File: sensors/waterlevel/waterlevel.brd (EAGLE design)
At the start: 100 x 80 mm, 57 parts, among them IC1 LD117AS33TR, IC2 MCP604SL, IC3 MCP601SN, IC4 MCP601SN, P1 CAMDEN-CTB5000/6, U1 NCP1729SN35T1G, U2 SR05S05, U3 VISHAY-VCUT05A4, U4 VISHAY-VCUT05A4

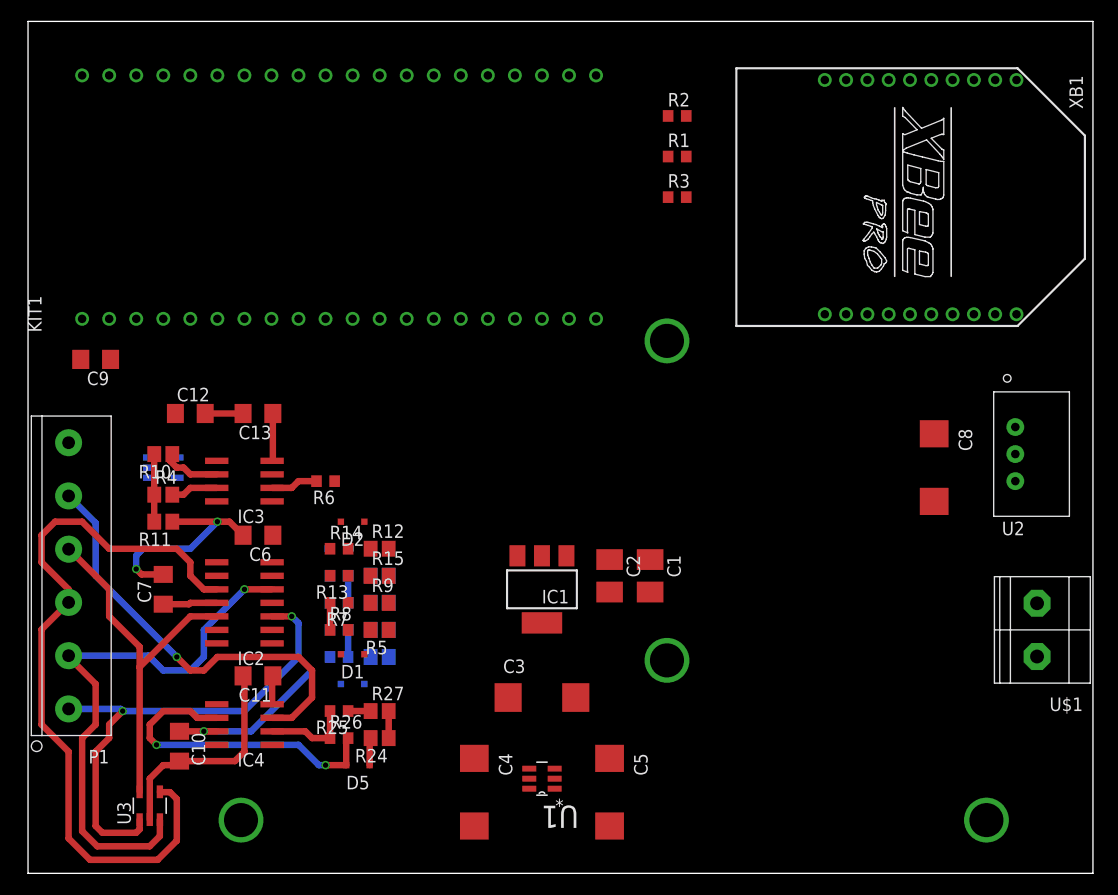
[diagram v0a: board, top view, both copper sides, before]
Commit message: Completed layout of water level sensor.
TODO:
Check circuit
Add status LEDs
Add bias resistors to GND
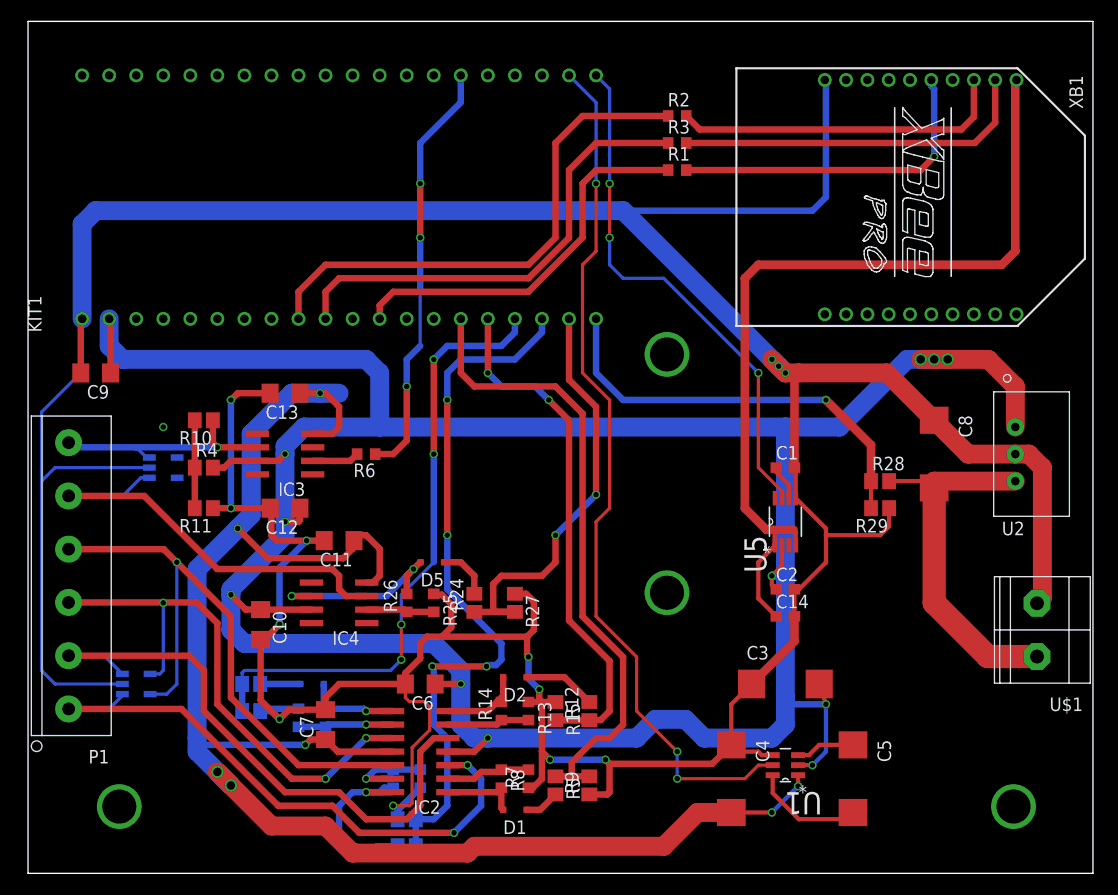
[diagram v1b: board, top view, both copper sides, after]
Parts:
- removed IC1: LD117AS33TR, v-reg:SOT223
- added C14: 2.2u, resistor:C0603
- added R28: 3k, resistor:R0805
- added R29: 1k, resistor:R0805
- added U5: LP3981IMM-3.3, eko-parts:SOP65P490X110-8N
- C1: value 10uF -> 33nF; device resistor:B/3528-21R -> resistor:C0603
- C2: value 10uF -> 2.2u; device resistor:B/3528-21R -> resistor:C0603
- moved R9 26.1 mm to (52.7, 8.26), turned to 90 degrees
- moved R12 24.9 mm to (52.7, 15.2), turned to 90 degrees
- moved R7 24.3 mm to (47.0, 8.89), turned to 90 degrees
- moved C4 24.2 mm to (66.0, 8.89)
- moved C3 22.9 mm to (71.1, 17.8)
- moved U1 22.9 mm to (71.1, 10.2)
- moved C5 22.9 mm to (77.5, 8.89)
- moved R5 22.0 mm to (49.5, 8.26), turned to 270 degrees
- moved R13 21.8 mm to (47.0, 15.2), turned to 270 degrees
- moved IC2 21.6 mm to (36.8, 11.4)
- moved R14 21.6 mm to (44.5, 15.2), turned to 90 degrees
- moved D2 21.1 mm to (45.7, 18.4)
- moved D1 21.1 mm to (45.7, 5.97)
- moved R15 20.8 mm to (49.5, 15.2), turned to 270 degrees
- moved R8 20.7 mm to (44.5, 8.89), turned to 270 degrees
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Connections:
- new net BAT_LVL: KIT1.P$20, R28.1, R29.2
- new net N$28: C1.1, U5.6
- new net N5V_ON: KIT1.P$22, U1.5
- new net XBEE_PWR_ON: KIT1.P$21, U5.7
- net +12V: now also R28.2
- net +3V3: now also C14.1, U5.1, U5.4; no longer C2.+, IC1.4
- net +5V: now also C2.1, U5.2; no longer C1.+, IC1.3, U1.5
- net GND: now also C1.2, C14.2, C2.2, R29.1, U5.5; no longer C1.-, C2.-, IC1.1
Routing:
- net GND: track 46.7 -> 419.8 mm, vias 2 -> 13
- net +5V: track 20.5 -> 271.5 mm, vias 1 -> 11
- net -5V: track 12.2 -> 158.9 mm, vias 0 -> 7
- net +3V3: track 0.00 -> 82.2 mm
- net N5V_ON: track 0.00 -> 81.8 mm, vias 0 -> 3
- net LVL4: track 0.00 -> 67.2 mm, vias 0 -> 4
- net LVL1: track 0.00 -> 61.2 mm
- net LVL3: track 0.00 -> 58.5 mm, vias 0 -> 4
- net LVL2: track 0.00 -> 52.0 mm, vias 0 -> 2
- net MBED_TX: track 0.00 -> 49.3 mm
- net XBEE_PWR_ON: track 0.00 -> 49.2 mm, vias 0 -> 3
- net MBED_RX: track 0.00 -> 44.2 mm
- net SQR_IN: track 0.00 -> 39.9 mm, vias 0 -> 3
- net BAT_LVL: track 0.00 -> 39.6 mm, vias 0 -> 1
- net LVL5: track 2.54 -> 40.6 mm, vias 0 -> 2
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
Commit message: Added LEDs and Bias Resistors to water sensor
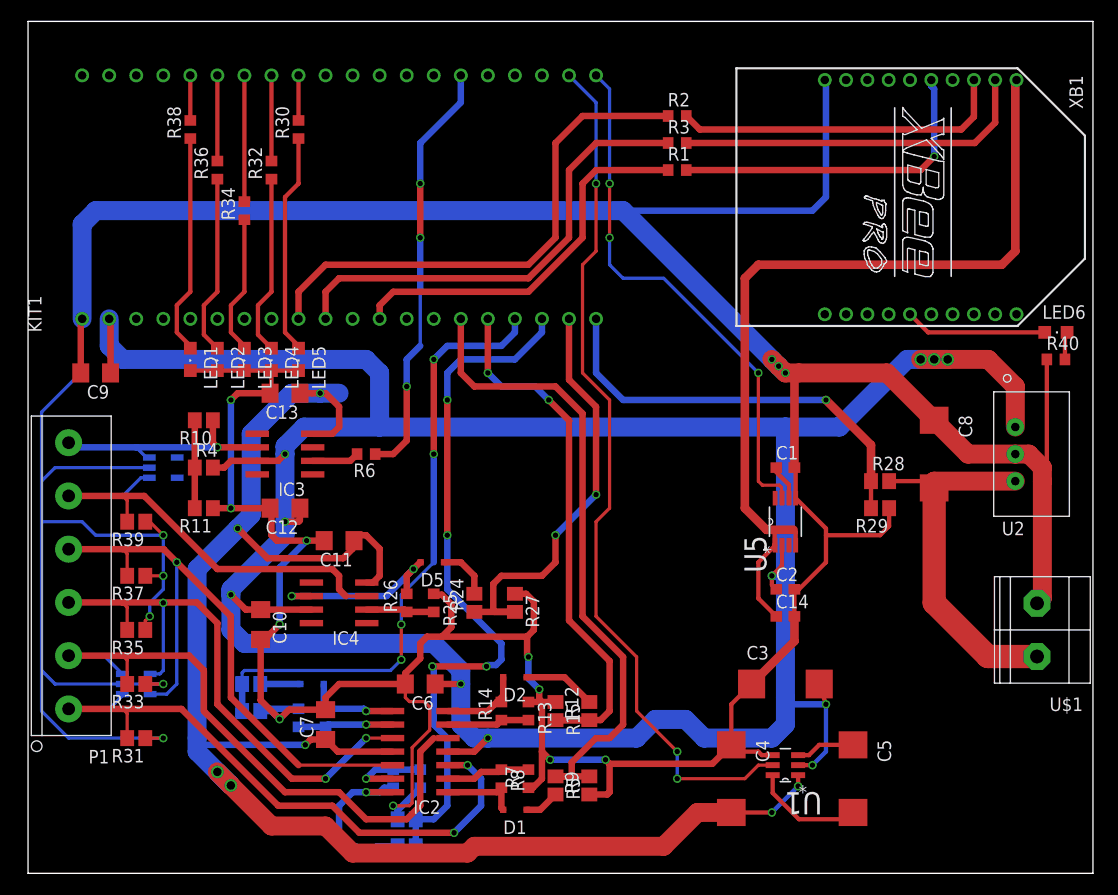
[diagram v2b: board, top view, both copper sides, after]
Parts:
- added LED1, LED2, LED3, LED4, LED5, LED6: (no value), led:CHIPLED_0805
- added R30, R32, R34, R36, R38, R40: (no value), resistor:R0603
- added R31, R33, R35, R37, R39: (no value), resistor:R0805
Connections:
- new net LED1: KIT1.RD-, R38.2
- new net LED2: KIT1.RD+, R36.2
- new net LED3: KIT1.TD-, R34.2
- new net LED4: KIT1.TD+, R32.2
- new net LED5: KIT1.D-, R30.2
- new net N$17: LED6.A, XB1.15
- new net N$24: LED6.C, R40.2
- new net N$25: LED5.A, R30.1
- new net N$26: LED4.A, R32.1
- new net N$27: LED3.A, R34.1
- new net N$29: LED2.A, R36.1
- new net N$30: LED1.A, R38.1
- net GND: now also LED1.C, LED2.C, LED3.C, LED4.C, LED5.C, R31.1, R33.1, R35.1, R37.1, R39.1, R40.1
- net SENSOR_IN_1: now also R31.2
- net SENSOR_IN_2: now also R33.2
- net SENSOR_IN_3: now also R35.2
- net SENSOR_IN_4: now also R37.2
- net SENSOR_IN_5: now also R39.2
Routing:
- net GND: track 419.8 -> 492.7 mm, vias 13 -> 18
- net N$30: track 0.00 -> 20.7 mm
- net N$25: track 0.00 -> 20.7 mm, vias 1 -> 0
- net N$29: track 0.00 -> 16.9 mm
- net N$26: track 0.00 -> 16.9 mm, vias 1 -> 0
- net N$17: track 0.00 -> 13.4 mm, vias 1 -> 0
- net N$27: track 0.00 -> 13.1 mm, vias 1 -> 0
- net LED3: track 0.00 -> 11.9 mm
- net LED4: track 0.00 -> 8.04 mm
- net LED2: track 0.00 -> 8.04 mm
- net LED5: track 0.00 -> 4.23 mm
- net LED1: track 0.00 -> 4.23 mm
- net SENSOR_IN_1: track 56.5 -> 59.4 mm
- net SENSOR_IN_2: track 56.1 -> 58.9 mm
- net SENSOR_IN_3: track 54.2 -> 57.0 mm
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
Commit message: Completed water level sensor / wireless network board.
Added status LEDs
Added test points for critical signals
Added M3 mounting holes
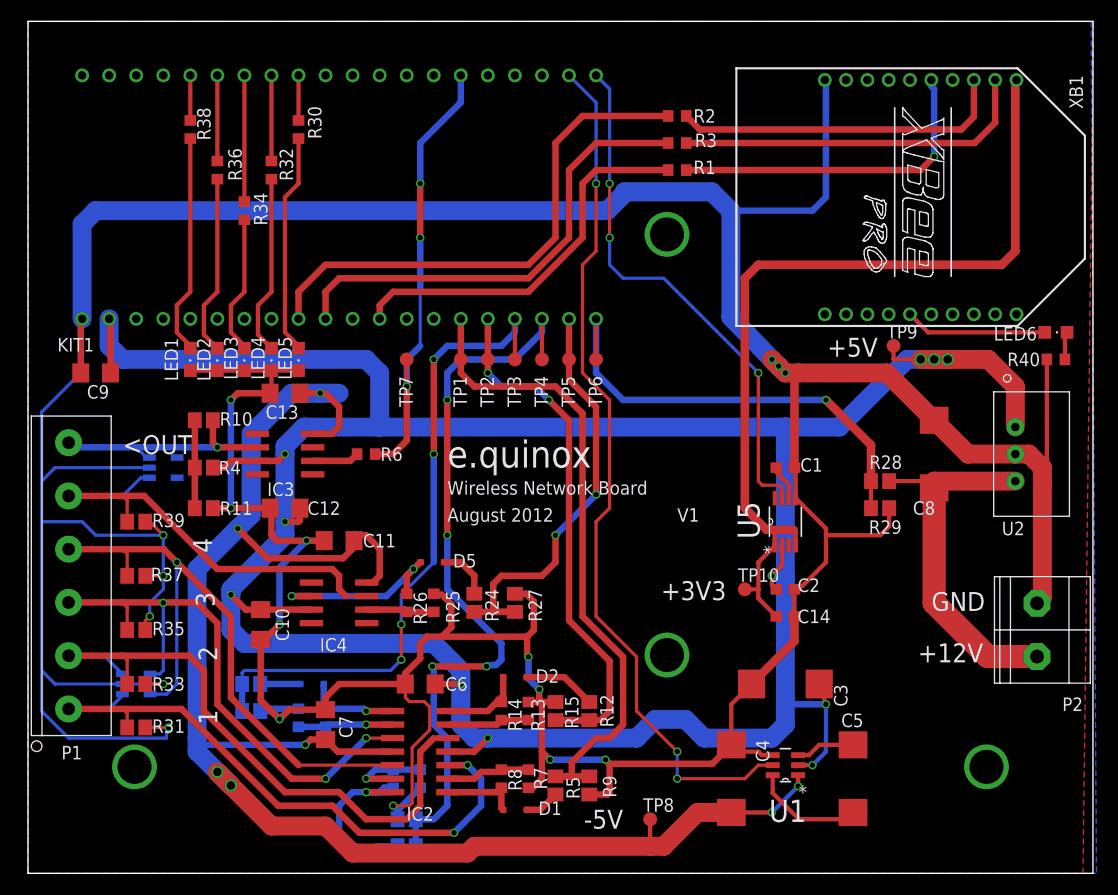
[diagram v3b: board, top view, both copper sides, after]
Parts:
- added TP1, TP10, TP2, TP3, TP4, TP5, TP6, TP7, TP8, TP9: TPTP13R, testpad:TP13R
- added U$2: (no value), eko-parts:EQNXLOGO
- moved R31 1.00 mm to (10.2, 13.7)
- renumbered U$1 to P2
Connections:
- net +3V3: now also TP10.TP
- net +5V: now also TP9.TP
- net -5V: now also TP8.TP
- net BAT_LVL: now also TP6.TP
- net LVL1: now also TP1.TP
- net LVL2: now also TP2.TP
- net LVL3: now also TP3.TP
- net LVL4: now also TP4.TP
- net LVL5: now also TP5.TP
- net SQR_IN: now also TP7.TP
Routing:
- net GND: track 492.7 -> 502.6 mm, vias 18 -> 22
- net LVL4: track 67.2 -> 71.0 mm
- net LVL3: track 58.5 -> 62.3 mm
- net BAT_LVL: track 39.6 -> 43.4 mm
- net +5V: track 271.5 -> 275.3 mm
- net SQR_IN: track 39.9 -> 42.4 mm
- net -5V: track 158.9 -> 161.4 mm
- net +3V3: track 82.2 -> 83.5 mm
- net SENSOR_IN_1: track 59.4 -> 58.4 mm
- added copper zone on layer 1, net GND
- added copper zone on layer 16, net GND
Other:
- board text added: "+12V"
- board text added: "+3V3"
- board text added: "+5V"
- board text added: "-5V"
- board text added: "1"
- board text added: "2"
- board text added: "3"
- board text added: "4"
- board text added: "<OUT"
- board text added: "August 2012"
- board text added: "GND"
- board text added: "V1"
- board text added: "Wireless Network Board"
- board text added: "e.quinox"

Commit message: [WSensor] Fixed bug with unconnected opamp input. Fixed component values.
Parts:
- C9: value (none) -> 1uF
- LED1: value (none) -> RED
- LED2: value (none) -> AMBER
- LED3, LED4, LED5: value (none) -> GREEN
- R1, R2, R3: value (none) -> 33
- R13, R17, R21, R25, R7: value (none) -> DNP
- R30, R32, R34, R36, R38, R40: value (none) -> 200
- R31, R33, R35, R37, R39: value (none) -> 1M
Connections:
- net N$23: now also IC3.3
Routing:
- net N$23: track 8.26 -> 22.2 mm
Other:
- board text added: "HI"
- board text added: "LO"
